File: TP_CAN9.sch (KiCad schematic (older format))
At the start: 1 part

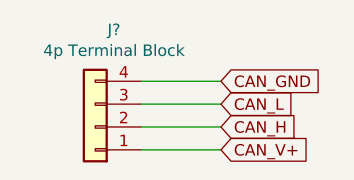
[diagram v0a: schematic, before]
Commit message: Add a tenth RJ10 connector.
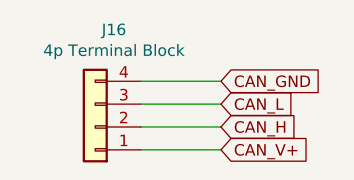
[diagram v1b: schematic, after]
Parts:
- gave numbers to parts that had none: 1
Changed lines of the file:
@@
 $Descr A4 11693 8268
 encoding utf-8
-Sheet 13 16
-Title ""
-Date ""
-Rev ""
+Sheet 16 16
+Title "CAN Distributor"
+Date "2021-04-03"
+Rev "2.0"
 Comp ""
-Comment1 ""
+Comment1 "Designed by: Erik Almbratt"
 Comment2 ""
 Comment3 ""
@@
 $EndDescr
 $Comp
-L Connector_Generic:Conn_01x04 J?
+L Connector_Generic:Conn_01x04 J13
 U 1 1 606A774B
 P 5300 3600
-AR Path="/606A6B6A/606A774B" Ref="J?"  Part="1"
-AR Path="/606A6E99/606A774B" Ref="J?"  Part="1"
-AR Path="/606A6FCD/606A774B" Ref="J?"  Part="1"
-AR Path="/606A70AE/606A774B" Ref="J?"  Part="1"
-F 0 "J?" H 5218 3175 50  0000 C CNN
+AR Path="/606A6B6A/606A774B" Ref="J13"  Part="1"
+AR Path="/606A6E99/606A774B" Ref="J14"  Part="1"
+AR Path="/606A6FCD/606A774B" Ref="J15"  Part="1"
+AR Path="/606A70AE/606A774B" Ref="J16"  Part="1"
+F 0 "J16" H 5218 3175 50  0000 C CNN
 F 1 "4p Terminal Block" H 5218 3266 50  0000 C CNN
 F 2 "TerminalBlock_TE-Connectivity:TerminalBlock_TE_282834-4_1x04_P2.54mm_Horizontal" H 5300 3600 50  0001 C CNN
